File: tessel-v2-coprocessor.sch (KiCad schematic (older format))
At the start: 38 parts, among them J401 CONN_02X05, J402 USB-micro-TH, J403 MODULE_HEADER, J404 MODULE_HEADER, SW401 SW_PUSH, U401 SAMD21G14A-MU, X401 FC-135

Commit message: annotation did not take?
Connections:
- wire segments 225 -> 194
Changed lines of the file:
@@
 	1800 5300 1800 5400
 Wire Wire Line
-	1500 5300 1500 5400
-Wire Wire Line
-	1500 5400 1500 5500
-Wire Wire Line
-	1500 4000 1500 4100
-Wire Wire Line
-	1500 4100 1500 4200
-Wire Wire Line
-	1500 4200 1500 4300
-Wire Wire Line
-	1500 4300 1500 4400
-Wire Wire Line
-	1500 4400 1500 4500
-Wire Wire Line
-	1500 4500 1500 4700
-Wire Wire Line
-	1500 4700 1500 4900
+	1500 5300 1500 5500
+Wire Wire Line
+	1500 4000 1500 4900
 Wire Wire Line
 	1800 4700 1500 4700
@@
 Connection ~ 3500 4250
 Wire Wire Line
-	2700 4250 3500 4250
-Wire Wire Line
-	3500 4250 4300 4250
-Wire Wire Line
-	2700 4150 3600 4150
-Wire Wire Line
-	3600 4150 4300 4150
+	2700 4250 4300 4250
+Wire Wire Line
+	2700 4150 4300 4150
 Wire Wire Line
 	2700 4050 2800 4050
@@
 	1600 2300 1600 2200
 Wire Wire Line
-	2200 2300 2300 2300
-Wire Wire Line
-	2300 2300 2950 2300
-Wire Wire Line
-	2200 2400 2350 2400
-Wire Wire Line
-	2350 2400 3200 2400
+	2200 2300 2950 2300
+Wire Wire Line
+	2200 2400 3200 2400
 Wire Wire Line
 	2400 2700 2200 2700
@@
 	1700 2400 1600 2400
 Wire Wire Line
-	1600 2400 1600 2500
-Wire Wire Line
-	1600 2500 1600 2900
+	1600 2400 1600 2900
 Wire Wire Line
 	1700 2500 1600 2500
@@
 	14700 6900 14700 6800
 Wire Wire Line
-	14300 6900 14600 6900
-Wire Wire Line
-	14600 6900 14700 6900
-Wire Wire Line
-	14700 6900 15500 6900
+	14300 6900 15500 6900
 Wire Wire Line
 	14550 6100 14700 6100
@@
 Connection ~ 2700 7300
 Wire Wire Line
-	2700 7200 2700 7300
-Wire Wire Line
-	2700 7300 2700 7400
+	2700 7200 2700 7400
 Wire Wire Line
 	1900 7300 2700 7300
@@
 	8200 7900 8200 7800
 Wire Wire Line
-	8000 7900 8200 7900
-Wire Wire Line
-	8200 7900 8300 7900
-Wire Wire Line
-	8300 7900 8400 7900
-Wire Wire Line
-	8400 7900 8600 7900
-Wire Wire Line
-	8000 7800 8000 7900
-Wire Wire Line
-	8000 7900 8000 8100
+	8000 7900 8600 7900
+Wire Wire Line
+	8000 7800 8000 8100
 Connection ~ 7500 3100
 Wire Wire Line
 	7500 3300 7500 3100
 Wire Wire Line
-	7600 2300 7900 2300
-Wire Wire Line
-	7900 2300 8300 2300
-Wire Wire Line
-	8300 2300 8400 2300
-Wire Wire Line
-	8400 2300 8600 2300
+	7600 2300 8600 2300
 Wire Wire Line
 	6900 4700 6250 4700
@@
 	4800 6700 6900 6700
 Wire Wire Line
-	5700 7300 6000 7300
-Wire Wire Line
-	6000 7300 6900 7300
+	5700 7300 6900 7300
 Wire Wire Line
 	9700 4600 10600 4600
@@
 	9700 7100 10600 7100
 Wire Wire Line
-	4800 6700 4800 7300
-Wire Wire Line
-	4800 7300 4800 7450
+	4800 6700 4800 7450
 Wire Wire Line
 	4800 7300 5100 7300
@@
 	4800 7850 4800 8000
 Wire Wire Line
-	8600 3000 8600 3100
-Wire Wire Line
-	8600 3100 8600 4200
-Wire Wire Line
-	8600 3100 9000 3100
-Wire Wire Line
-	9000 3100 9400 3100
+	8600 3000 8600 4200
+Wire Wire Line
+	8600 3100 9400 3100
 Wire Wire Line
 	9000 3100 9000 3300
 Wire Wire Line
-	9400 2950 9400 3100
-Wire Wire Line
-	9400 3100 9400 3300
+	9400 2950 9400 3300
 Connection ~ 9000 3100
 Connection ~ 8600 3100
 Wire Wire Line
-	7100 3100 7500 3100
-Wire Wire Line
-	7500 3100 7900 3100
+	7100 3100 7900 3100
 Wire Wire Line
 	7100 3100 7100 3300
@@
 	8100 3000 8100 4200
 Wire Wire Line
-	8300 2300 8300 2900
-Wire Wire Line
-	8300 2900 8300 4200
+	8300 2300 8300 4200
 Wire Wire Line
 	8300 2900 6300 2900
@@
 	7600 2300 7600 2150
 Wire Wire Line
-	8400 2300 8400 2800
-Wire Wire Line
-	8400 2800 8400 4200
+	8400 2300 8400 4200
 Connection ~ 8400 2300
 Connection ~ 8400 2800
@@
 Connection ~ 8300 2900
 Wire Wire Line
-	7900 2300 7900 3100
-Wire Wire Line
-	7900 3100 7900 4200
+	7900 2300 7900 4200
 Connection ~ 7900 2300
 Connection ~ 7900 3100

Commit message: post-quick review from refactor
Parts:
- removed C402: 100nF, tm-kicad-lib:SMD-0402-C, symbol C
- renumbered C403 to C402, C404 to C403, C405 to C404, C406 to C405, C407 to C406, C408 to C407, C409 to C408, C410 to C409, C411 to C410, C412 to C411, R403 to R402, R404 to R403, R405 to R404, R406 to R405, R402 to R406
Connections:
- wire segments 194 -> 192
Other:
- moved on the sheet: R406

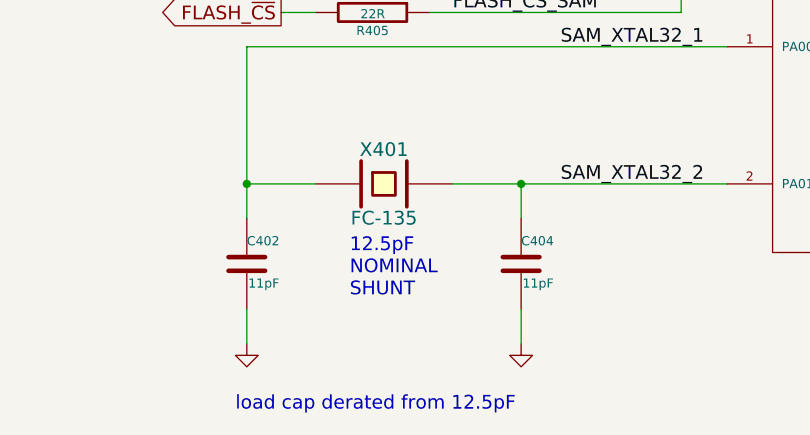
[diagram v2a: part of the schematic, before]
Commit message: value optimization for the sake of bom complexity
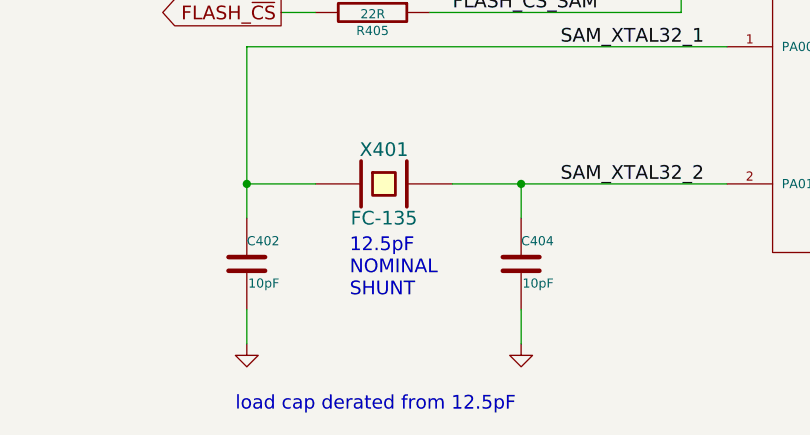
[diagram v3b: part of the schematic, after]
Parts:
- C402, C404: value 11pF -> 10pF
- SW401: footprint (none) -> !Parts:TL1015AF160QG
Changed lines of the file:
@@
 P 6000 7650
 F 0 "C404" H 6000 7750 40  0000 L CNN
-F 1 "11pF" H 6006 7565 40  0000 L CNN
+F 1 "10pF" H 6006 7565 40  0000 L CNN
 F 2 "tm-kicad-lib:SMD-0402-C" H 6038 7500 30  0001 C CNN
 F 3 "" H 6000 7650 60  0000 C CNN
@@
 P 4800 7650
 F 0 "C402" H 4800 7750 40  0000 L CNN
-F 1 "11pF" H 4806 7565 40  0000 L CNN
+F 1 "10pF" H 4806 7565 40  0000 L CNN
 F 2 "tm-kicad-lib:SMD-0402-C" H 4838 7500 30  0001 C CNN
 F 3 "" H 4800 7650 60  0000 C CNN
@@
 	1    0    0    -1
 $EndComp
-Text Notes 5250 7800 0    60   ~ 0
-12.5pF\nNOMINAL\nSHUNT
 $Comp
 L C C408
@@
 Text Label 5700 6550 0    60   ~ 0
 FLASH_~CS~_SAM
-Text Notes 4750 8300 0    60   ~ 0
-load cap derated from 12.5pF
 Text Label 5700 6000 0    60   ~ 0
 BUTTON
@@
 F 0 "SW401" H 14150 7010 50  0000 C CNN
 F 1 "SW_PUSH" H 14000 6820 50  0000 C CNN
-F 2 "" H 14000 6900 60  0000 C CNN
+F 2 "!Parts:TL1015AF160QG" H 14000 6900 60  0001 C CNN
 F 3 "" H 14000 6900 60  0000 C CNN
 	1    14000 6900
@@
 	5500 4600 5500 4700
 Connection ~ 5500 4700
+Text Notes 4750 8300 0    60   ~ 0
+load cap derated from 12.5pF
+Text Notes 5250 7800 0    60   ~ 0
+12.5pF\nNOMINAL\nSHUNT
 $EndSCHEMATC

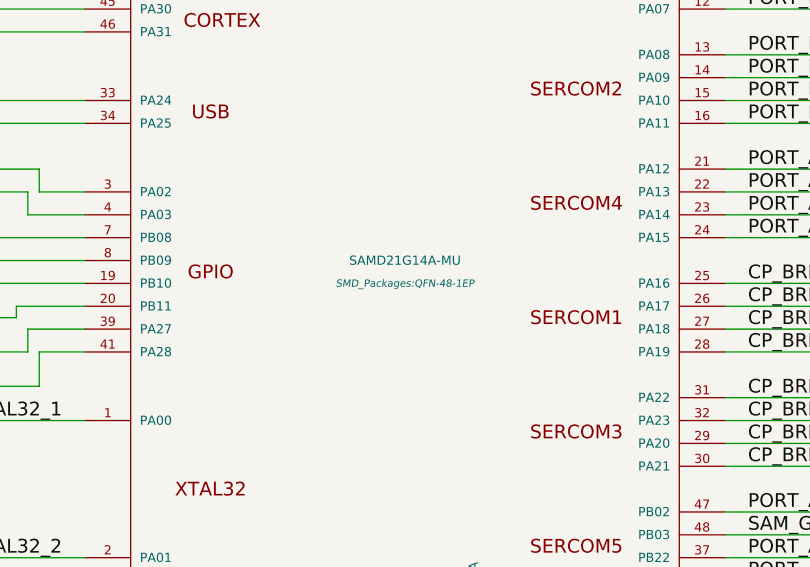
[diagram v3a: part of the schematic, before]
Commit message: 1) can't believe i started from scratch 2) single best feature in today's kicad build: allign/distribute.
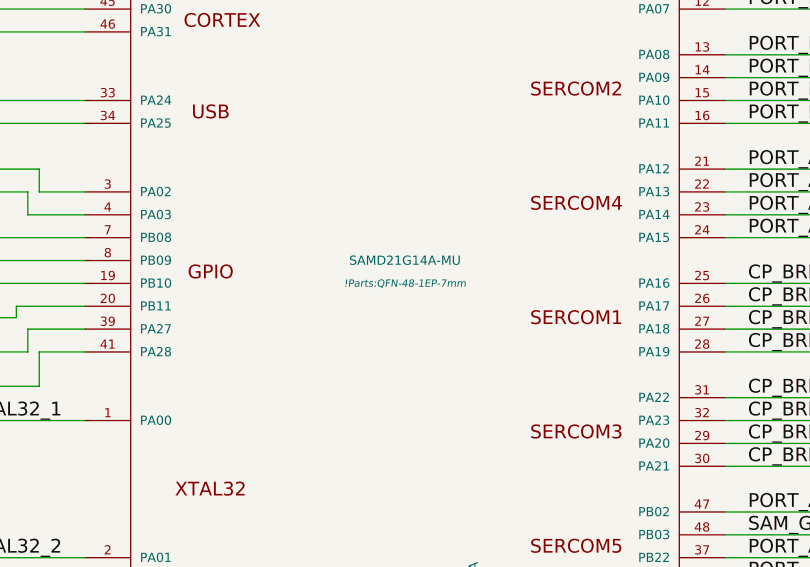
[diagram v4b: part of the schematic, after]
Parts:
- U401: footprint SMD_Packages:QFN-48-1EP -> !Parts:QFN-48-1EP-7mm
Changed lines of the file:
@@
 $EndComp
 $Comp
-L GND #PWR0110
+L GND #PWR407
 U 1 1 548F9730
 P 4800 8000
-F 0 "#PWR0110" H 4800 8000 30  0001 C CNN
+F 0 "#PWR407" H 4800 8000 30  0001 C CNN
 F 1 "GND" H 4800 7930 30  0001 C CNN
 F 2 "" H 4800 8000 60  0000 C CNN
@@
 $EndComp
 $Comp
-L GND #PWR0111
+L GND #PWR409
 U 1 1 548F973F
 P 6000 8000
-F 0 "#PWR0111" H 6000 8000 30  0001 C CNN
+F 0 "#PWR409" H 6000 8000 30  0001 C CNN
 F 1 "GND" H 6000 7930 30  0001 C CNN
 F 2 "" H 6000 8000 60  0000 C CNN
@@
 F 0 "U401" H 7150 7650 40  0000 C CNN
 F 1 "SAMD21G14A-MU" H 8300 6000 40  0000 C CNN
-F 2 "SMD_Packages:QFN-48-1EP" H 8300 5900 32  0000 C CIN
+F 2 "!Parts:QFN-48-1EP-7mm" H 8300 5900 32  0000 C CIN
 F 3 "" H 7100 5650 60  0000 C CNN
 	1    8300 6000
@@
 VDDCORE
 $Comp
-L GND #PWR0112
+L GND #PWR416
 U 1 1 548FA205
 P 9400 3900
-F 0 "#PWR0112" H 9400 3900 30  0001 C CNN
+F 0 "#PWR416" H 9400 3900 30  0001 C CNN
 F 1 "GND" H 9400 3830 30  0001 C CNN
 F 2 "" H 9400 3900 60  0000 C CNN
@@
 $EndComp
 $Comp
-L GND #PWR0113
+L GND #PWR415
 U 1 1 548FBD70
 P 9000 3900
-F 0 "#PWR0113" H 9000 3900 30  0001 C CNN
+F 0 "#PWR415" H 9000 3900 30  0001 C CNN
 F 1 "GND" H 9000 3830 30  0001 C CNN
 F 2 "" H 9000 3900 60  0000 C CNN
@@
 $EndComp
 $Comp
-L GND #PWR0114
+L GND #PWR413
 U 1 1 548FBD83
 P 7500 3900
-F 0 "#PWR0114" H 7500 3900 30  0001 C CNN
+F 0 "#PWR413" H 7500 3900 30  0001 C CNN
 F 1 "GND" H 7500 3830 30  0001 C CNN
 F 2 "" H 7500 3900 60  0000 C CNN
@@
 $EndComp
 $Comp
-L GND #PWR0115
+L GND #PWR412
 U 1 1 548FBD8A
 P 7100 3900
-F 0 "#PWR0115" H 7100 3900 30  0001 C CNN
+F 0 "#PWR412" H 7100 3900 30  0001 C CNN
 F 1 "GND" H 7100 3830 30  0001 C CNN
 F 2 "" H 7100 3900 60  0000 C CNN
@@
 $EndComp
 $Comp
-L GND #PWR0116
+L GND #PWR411
 U 1 1 548FBD9D
 P 6700 3900
-F 0 "#PWR0116" H 6700 3900 30  0001 C CNN
+F 0 "#PWR411" H 6700 3900 30  0001 C CNN
 F 1 "GND" H 6700 3830 30  0001 C CNN
 F 2 "" H 6700 3900 60  0000 C CNN
@@
 $EndComp
 $Comp
-L GND #PWR0117
+L GND #PWR410
 U 1 1 548FBDA4
 P 6300 3900
-F 0 "#PWR0117" H 6300 3900 30  0001 C CNN
+F 0 "#PWR410" H 6300 3900 30  0001 C CNN
 F 1 "GND" H 6300 3830 30  0001 C CNN
 F 2 "" H 6300 3900 60  0000 C CNN
@@
 $EndComp
 $Comp
-L GND #PWR0118
+L GND #PWR408
 U 1 1 548FBDB7
 P 5900 3900
-F 0 "#PWR0118" H 5900 3900 30  0001 C CNN
+F 0 "#PWR408" H 5900 3900 30  0001 C CNN
 F 1 "GND" H 5900 3830 30  0001 C CNN
 F 2 "" H 5900 3900 60  0000 C CNN
@@
 $EndComp
 $Comp
-L GND #PWR0119
+L GND #PWR414
 U 1 1 548FD791
 P 8000 8100
-F 0 "#PWR0119" H 8000 8100 30  0001 C CNN
+F 0 "#PWR414" H 8000 8100 30  0001 C CNN
 F 1 "GND" H 8000 8030 30  0001 C CNN
 F 2 "" H 8000 8100 60  0000 C CNN
@@
 $EndComp
 $Comp
-L GND #PWR0120
+L GND #PWR421
 U 1 1 54E6B173
 P 14600 7500
-F 0 "#PWR0120" H 14600 7500 30  0001 C CNN
+F 0 "#PWR421" H 14600 7500 30  0001 C CNN
 F 1 "GND" H 14600 7430 30  0001 C CNN
 F 2 "" H 14600 7500 60  0000 C CNN
@@
 3.3V_CP
 $Comp
-L GND #PWR0121
+L GND #PWR418
 U 1 1 54E6B4A0
 P 13600 7500
-F 0 "#PWR0121" H 13600 7500 30  0001 C CNN
+F 0 "#PWR418" H 13600 7500 30  0001 C CNN
 F 1 "GND" H 13600 7430 30  0001 C CNN
 F 2 "" H 13600 7500 60  0000 C CNN
@@
 NoConn ~ 1700 2700
 $Comp
-L GND #PWR0122
+L GND #PWR402
 U 1 1 54E6D866
 P 1600 2900
-F 0 "#PWR0122" H 1600 2650 60  0001 C CNN
+F 0 "#PWR402" H 1600 2650 60  0001 C CNN
 F 1 "GND" H 1600 2750 60  0000 C CNN
 F 2 "" H 1600 2900 60  0000 C CNN
@@
 3.3V_PORTA
 $Comp
-L GND #PWR0123
+L GND #PWR419
 U 1 1 54E753B7
 P 14200 2400
-F 0 "#PWR0123" H 14200 2150 60  0001 C CNN
+F 0 "#PWR419" H 14200 2150 60  0001 C CNN
 F 1 "GND" H 14200 2250 60  0000 C CNN
 F 2 "" H 14200 2400 60  0000 C CNN
@@
 $EndComp
 $Comp
-L GND #PWR0124
+L GND #PWR420
 U 1 1 54E753CD
 P 14300 4200
-F 0 "#PWR0124" H 14300 3950 60  0001 C CNN
+F 0 "#PWR420" H 14300 3950 60  0001 C CNN
 F 1 "GND" H 14300 4050 60  0000 C CNN
 F 2 "" H 14300 4200 60  0000 C CNN
@@
 PORT_A_G3
 $Comp
-L +5V #PWR0125
+L +5V #PWR403
 U 1 1 54E79A0D
 P 2800 3900
-F 0 "#PWR0125" H 2800 3990 20  0001 C CNN
+F 0 "#PWR403" H 2800 3990 20  0001 C CNN
 F 1 "+5V" H 2800 4050 30  0000 C CNN
 F 2 "" H 2800 3900 60  0000 C CNN
@@
 $EndComp
 $Comp
-L GND #PWR0126
+L GND #PWR404
 U 1 1 54E79A13
 P 2800 4600
-F 0 "#PWR0126" H 2800 4350 60  0001 C CNN
+F 0 "#PWR404" H 2800 4350 60  0001 C CNN
 F 1 "GND" H 2800 4450 60  0000 C CNN
 F 2 "" H 2800 4600 60  0000 C CNN
@@
 $EndComp
 $Comp
-L GND #PWR0127
+L GND #PWR405
 U 1 1 54E79A19
 P 3100 5000
-F 0 "#PWR0127" H 3100 4750 60  0001 C CNN
+F 0 "#PWR405" H 3100 4750 60  0001 C CNN
 F 1 "GND" H 3100 4850 60  0000 C CNN
 F 2 "" H 3100 5000 60  0000 C CNN
@@
 $EndComp
 $Comp
-L GND #PWR0128
+L GND #PWR401
 U 1 1 54E79A1F
 P 1500 5500
-F 0 "#PWR0128" H 1500 5250 60  0001 C CNN
+F 0 "#PWR401" H 1500 5250 60  0001 C CNN
 F 1 "GND" H 1500 5350 60  0000 C CNN
 F 2 "" H 1500 5500 60  0000 C CNN
@@
 $EndComp
 $Comp
-L +5V #PWR0129
+L +5V #PWR406
 U 1 1 54E79A2D
 P 4000 4600
-F 0 "#PWR0129" H 4000 4690 20  0001 C CNN
+F 0 "#PWR406" H 4000 4690 20  0001 C CNN
 F 1 "+5V" H 4000 4750 30  0000 C CNN
 F 2 "" H 4000 4600 60  0000 C CNN
@@
 FLASH_~CS
 $Comp
-L GND #PWR0130
+L GND #PWR417
 U 1 1 54EE1D18
 P 12300 3700
-F 0 "#PWR0130" H 12300 3450 60  0001 C CNN
+F 0 "#PWR417" H 12300 3450 60  0001 C CNN
 F 1 "GND" H 12300 3550 60  0000 C CNN
 F 2 "" H 12300 3700 60  0000 C CNN

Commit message: sadly, we may need to rotate the mediatek...
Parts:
- C408, C409: footprint SMD_Packages:SMD-0805 -> tm-kicad-lib:SMD-0805-C
- SW401: footprint !Parts:TL1015AF160QG -> tm-kicad-lib:TL1015AF160QG
- U401: footprint !Parts:QFN-48-1EP-7mm -> tm-kicad-lib:QFN-48-1EP-7mm
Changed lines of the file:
@@
 $EndComp
 $Comp
-L GND #PWR407
+L GND #PWR0110
 U 1 1 548F9730
 P 4800 8000
-F 0 "#PWR407" H 4800 8000 30  0001 C CNN
+F 0 "#PWR0110" H 4800 8000 30  0001 C CNN
 F 1 "GND" H 4800 7930 30  0001 C CNN
 F 2 "" H 4800 8000 60  0000 C CNN
@@
 $EndComp
 $Comp
-L GND #PWR409
+L GND #PWR0111
 U 1 1 548F973F
 P 6000 8000
-F 0 "#PWR409" H 6000 8000 30  0001 C CNN
+F 0 "#PWR0111" H 6000 8000 30  0001 C CNN
 F 1 "GND" H 6000 7930 30  0001 C CNN
 F 2 "" H 6000 8000 60  0000 C CNN
@@
 F 0 "C408" H 7500 3600 40  0000 L CNN
 F 1 "10uF" H 7506 3415 40  0000 L CNN
-F 2 "SMD_Packages:SMD-0805" H 7538 3350 30  0001 C CNN
+F 2 "tm-kicad-lib:SMD-0805-C" H 7538 3350 30  0001 C CNN
 F 3 "" H 7500 3500 60  0000 C CNN
 	1    7500 3500
@@
 F 0 "C409" H 9000 3600 40  0000 L CNN
 F 1 "10uF" H 9006 3415 40  0000 L CNN
-F 2 "SMD_Packages:SMD-0805" H 9038 3350 30  0001 C CNN
+F 2 "tm-kicad-lib:SMD-0805-C" H 9038 3350 30  0001 C CNN
 F 3 "" H 9000 3500 60  0000 C CNN
 	1    9000 3500
@@
 F 0 "U401" H 7150 7650 40  0000 C CNN
 F 1 "SAMD21G14A-MU" H 8300 6000 40  0000 C CNN
-F 2 "!Parts:QFN-48-1EP-7mm" H 8300 5900 32  0000 C CIN
+F 2 "tm-kicad-lib:QFN-48-1EP-7mm" H 8300 5900 32  0000 C CIN
 F 3 "" H 7100 5650 60  0000 C CNN
 	1    8300 6000
@@
 VDDCORE
 $Comp
-L GND #PWR416
+L GND #PWR0112
 U 1 1 548FA205
 P 9400 3900
-F 0 "#PWR416" H 9400 3900 30  0001 C CNN
+F 0 "#PWR0112" H 9400 3900 30  0001 C CNN
 F 1 "GND" H 9400 3830 30  0001 C CNN
 F 2 "" H 9400 3900 60  0000 C CNN
@@
 $EndComp
 $Comp
-L GND #PWR415
+L GND #PWR0113
 U 1 1 548FBD70
 P 9000 3900
-F 0 "#PWR415" H 9000 3900 30  0001 C CNN
+F 0 "#PWR0113" H 9000 3900 30  0001 C CNN
 F 1 "GND" H 9000 3830 30  0001 C CNN
 F 2 "" H 9000 3900 60  0000 C CNN
@@
 $EndComp
 $Comp
-L GND #PWR413
+L GND #PWR0114
 U 1 1 548FBD83
 P 7500 3900
-F 0 "#PWR413" H 7500 3900 30  0001 C CNN
+F 0 "#PWR0114" H 7500 3900 30  0001 C CNN
 F 1 "GND" H 7500 3830 30  0001 C CNN
 F 2 "" H 7500 3900 60  0000 C CNN
@@
 $EndComp
 $Comp
-L GND #PWR412
+L GND #PWR0115
 U 1 1 548FBD8A
 P 7100 3900
-F 0 "#PWR412" H 7100 3900 30  0001 C CNN
+F 0 "#PWR0115" H 7100 3900 30  0001 C CNN
 F 1 "GND" H 7100 3830 30  0001 C CNN
 F 2 "" H 7100 3900 60  0000 C CNN
@@
 $EndComp
 $Comp
-L GND #PWR411
+L GND #PWR0116
 U 1 1 548FBD9D
 P 6700 3900
-F 0 "#PWR411" H 6700 3900 30  0001 C CNN
+F 0 "#PWR0116" H 6700 3900 30  0001 C CNN
 F 1 "GND" H 6700 3830 30  0001 C CNN
 F 2 "" H 6700 3900 60  0000 C CNN
@@
 $EndComp
 $Comp
-L GND #PWR410
+L GND #PWR0117
 U 1 1 548FBDA4
 P 6300 3900
-F 0 "#PWR410" H 6300 3900 30  0001 C CNN
+F 0 "#PWR0117" H 6300 3900 30  0001 C CNN
 F 1 "GND" H 6300 3830 30  0001 C CNN
 F 2 "" H 6300 3900 60  0000 C CNN
@@
 $EndComp
 $Comp
-L GND #PWR408
+L GND #PWR0118
 U 1 1 548FBDB7
 P 5900 3900
-F 0 "#PWR408" H 5900 3900 30  0001 C CNN
+F 0 "#PWR0118" H 5900 3900 30  0001 C CNN
 F 1 "GND" H 5900 3830 30  0001 C CNN
 F 2 "" H 5900 3900 60  0000 C CNN
@@
 $EndComp
 $Comp
-L GND #PWR414
+L GND #PWR0119
 U 1 1 548FD791
 P 8000 8100
-F 0 "#PWR414" H 8000 8100 30  0001 C CNN
+F 0 "#PWR0119" H 8000 8100 30  0001 C CNN
 F 1 "GND" H 8000 8030 30  0001 C CNN
 F 2 "" H 8000 8100 60  0000 C CNN
@@
 F 0 "SW401" H 14150 7010 50  0000 C CNN
 F 1 "SW_PUSH" H 14000 6820 50  0000 C CNN
-F 2 "!Parts:TL1015AF160QG" H 14000 6900 60  0001 C CNN
+F 2 "tm-kicad-lib:TL1015AF160QG" H 14000 6900 60  0001 C CNN
 F 3 "" H 14000 6900 60  0000 C CNN
 	1    14000 6900
@@
 $EndComp
 $Comp
-L GND #PWR421
+L GND #PWR0120
 U 1 1 54E6B173
 P 14600 7500
-F 0 "#PWR421" H 14600 7500 30  0001 C CNN
+F 0 "#PWR0120" H 14600 7500 30  0001 C CNN
 F 1 "GND" H 14600 7430 30  0001 C CNN
 F 2 "" H 14600 7500 60  0000 C CNN
@@
 3.3V_CP
 $Comp
-L GND #PWR418
+L GND #PWR0121
 U 1 1 54E6B4A0
 P 13600 7500
-F 0 "#PWR418" H 13600 7500 30  0001 C CNN
+F 0 "#PWR0121" H 13600 7500 30  0001 C CNN
 F 1 "GND" H 13600 7430 30  0001 C CNN
 F 2 "" H 13600 7500 60  0000 C CNN
@@
 NoConn ~ 1700 2700
 $Comp
-L GND #PWR402
+L GND #PWR0122
 U 1 1 54E6D866
 P 1600 2900
-F 0 "#PWR402" H 1600 2650 60  0001 C CNN
+F 0 "#PWR0122" H 1600 2650 60  0001 C CNN
 F 1 "GND" H 1600 2750 60  0000 C CNN
 F 2 "" H 1600 2900 60  0000 C CNN
@@
 3.3V_PORTA
 $Comp
-L GND #PWR419
+L GND #PWR0123
 U 1 1 54E753B7
 P 14200 2400
-F 0 "#PWR419" H 14200 2150 60  0001 C CNN
+F 0 "#PWR0123" H 14200 2150 60  0001 C CNN
 F 1 "GND" H 14200 2250 60  0000 C CNN
 F 2 "" H 14200 2400 60  0000 C CNN
@@
 $EndComp
 $Comp
-L GND #PWR420
+L GND #PWR0124
 U 1 1 54E753CD
 P 14300 4200
-F 0 "#PWR420" H 14300 3950 60  0001 C CNN
+F 0 "#PWR0124" H 14300 3950 60  0001 C CNN
 F 1 "GND" H 14300 4050 60  0000 C CNN
 F 2 "" H 14300 4200 60  0000 C CNN
@@
 PORT_A_G3
 $Comp
-L +5V #PWR403
+L +5V #PWR0125
 U 1 1 54E79A0D
 P 2800 3900
-F 0 "#PWR403" H 2800 3990 20  0001 C CNN
+F 0 "#PWR0125" H 2800 3990 20  0001 C CNN
 F 1 "+5V" H 2800 4050 30  0000 C CNN
 F 2 "" H 2800 3900 60  0000 C CNN
@@
 $EndComp
 $Comp
-L GND #PWR404
+L GND #PWR0126
 U 1 1 54E79A13
 P 2800 4600
-F 0 "#PWR404" H 2800 4350 60  0001 C CNN
+F 0 "#PWR0126" H 2800 4350 60  0001 C CNN
 F 1 "GND" H 2800 4450 60  0000 C CNN
 F 2 "" H 2800 4600 60  0000 C CNN
@@
 $EndComp
 $Comp
-L GND #PWR405
+L GND #PWR0127
 U 1 1 54E79A19
 P 3100 5000
-F 0 "#PWR405" H 3100 4750 60  0001 C CNN
+F 0 "#PWR0127" H 3100 4750 60  0001 C CNN
 F 1 "GND" H 3100 4850 60  0000 C CNN
 F 2 "" H 3100 5000 60  0000 C CNN
@@
 $EndComp
 $Comp
-L GND #PWR401
+L GND #PWR0128
 U 1 1 54E79A1F
 P 1500 5500
-F 0 "#PWR401" H 1500 5250 60  0001 C CNN
+F 0 "#PWR0128" H 1500 5250 60  0001 C CNN
 F 1 "GND" H 1500 5350 60  0000 C CNN
 F 2 "" H 1500 5500 60  0000 C CNN
@@
 $EndComp
 $Comp
-L +5V #PWR406
+L +5V #PWR0129
 U 1 1 54E79A2D
 P 4000 4600
-F 0 "#PWR406" H 4000 4690 20  0001 C CNN
+F 0 "#PWR0129" H 4000 4690 20  0001 C CNN
 F 1 "+5V" H 4000 4750 30  0000 C CNN
 F 2 "" H 4000 4600 60  0000 C CNN
@@
 FLASH_~CS
 $Comp
-L GND #PWR417
+L GND #PWR0130
 U 1 1 54EE1D18
 P 12300 3700
-F 0 "#PWR417" H 12300 3450 60  0001 C CNN
+F 0 "#PWR0130" H 12300 3450 60  0001 C CNN
 F 1 "GND" H 12300 3550 60  0000 C CNN
 F 2 "" H 12300 3700 60  0000 C CNN
